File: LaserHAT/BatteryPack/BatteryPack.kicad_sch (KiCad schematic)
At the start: 140 parts, among them J1 TYPE-C-31-M-12, J3 B4B-PH-K-S(LF)(SN), J5 S5B-XH-A-1(LF)(SN), J6 S5B-XH-A-1(LF)(SN), J7 XT60PW-M, J8 XT60PW-M, Q1 AO3401A, Q10 AO3400A, Q11 AO3400A, Q12 AO3400A, Q13 AO3401A, Q14 AO3400A, Q15 AO3400A, Q16 AO3400A, Q17 AO3400A, Q18 AO3400A, Q6 AO3401A, Q7 AO3400A, Q8 AO3400A, Q9 AO3400A, SW1 CAX-MTS203M-YB-10.6JL, U1 LM393DR2G, U10 HY2213-BB3A, U11 HY2213-BB3A, U12 HY2213-BB3A, U13 HY2213-BB3A, U14 LM393DR2G, U15 LM393DR2G, U16 CJ431, U2 LM393DR2G, U3 CJ431, U4 CH224A, U5 CN3704, U6 HY2213-BB3A, U7 HY2213-BB3A, U8 HY2213-BB3A, U9 HY2213-BB3A

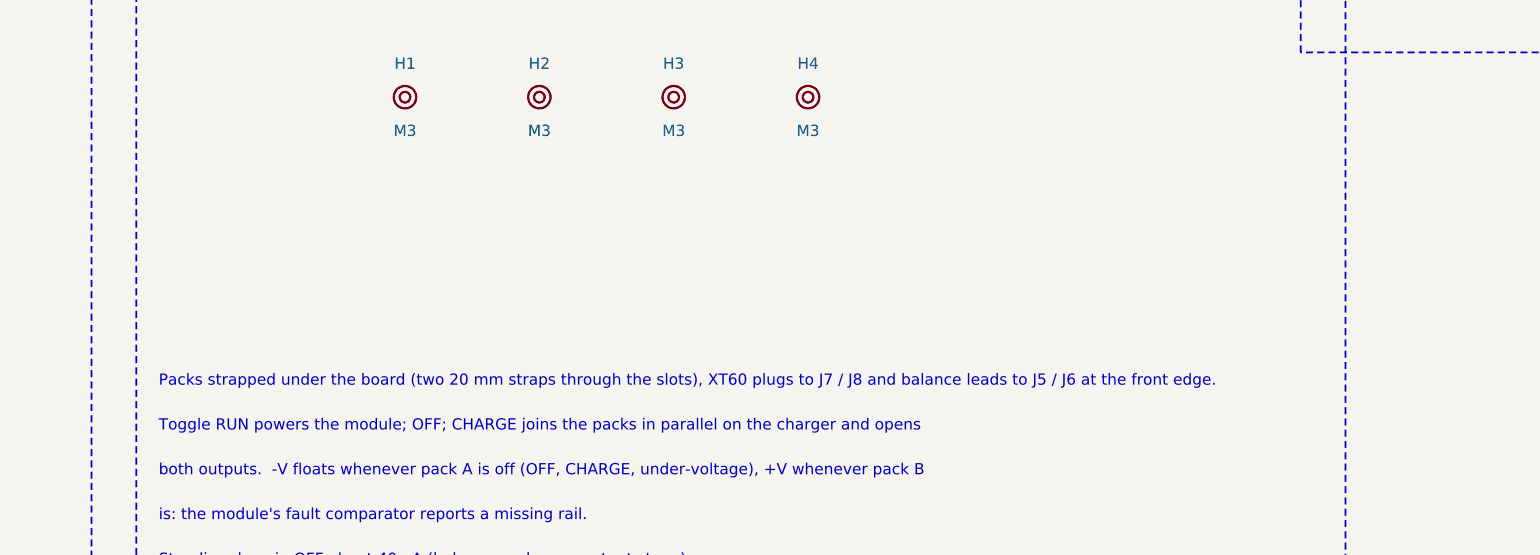
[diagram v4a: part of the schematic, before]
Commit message: BatteryPack: Raspberry Pi mounting holes (H5-H8, 58 x 49 M2.5) so the Pi + HAT sit above the board
Pi over y 4-60 on standoffs, ports end 11 mm past the right edge; toggle, pack sockets, output header and every
LED stay uncovered.  Balancer rows up 3 mm (pack B 1 mm left), CHRG / DONE LEDs to the top edge outside the Pi,
R9-R11 and C3 nudged, no-via rule areas under the standoffs.  Re-routed; one +SW pad entry hand-fixed for the
0.2 mm clearance.  DRC 0 / 0 / 0, ERC 0, path / sync 0, fab 136 placements / 44 BOM lines.

Co-Authored-By: Claude Fable 5.1 <noreply@anthropic.com>
Claude-Session: https://claude.ai/code/session_018vgLizGzYPynnY93ajvoVA
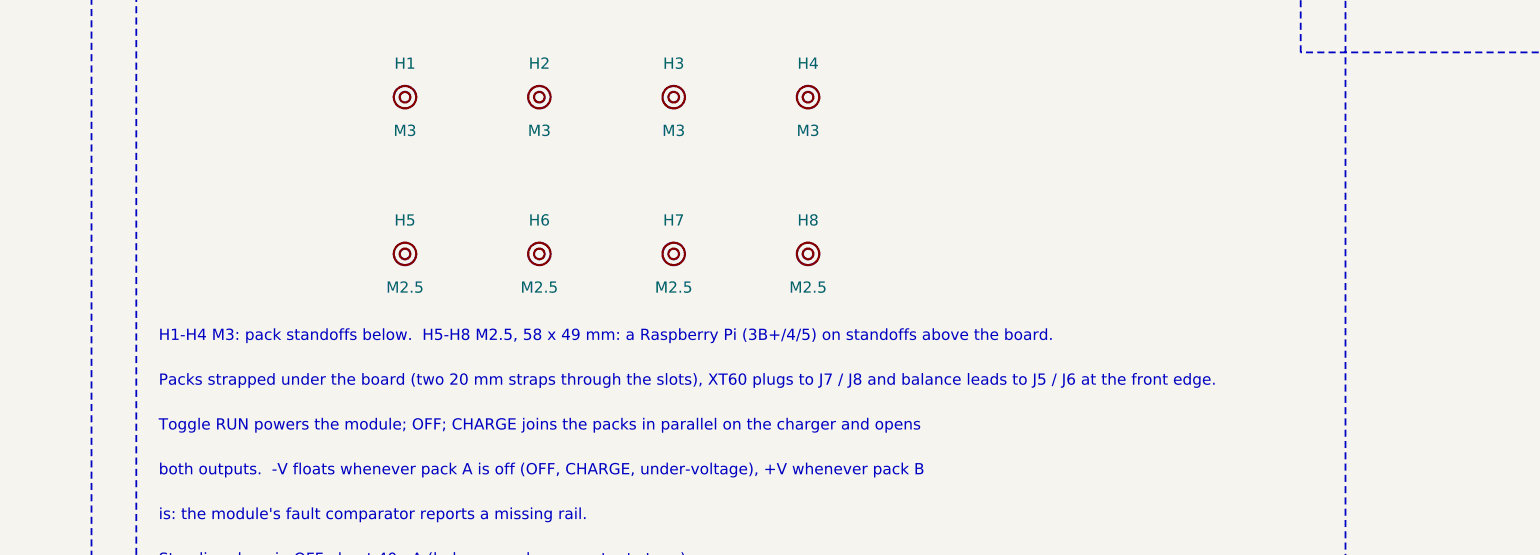
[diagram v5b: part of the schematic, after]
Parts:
- added H5, H6, H7, H8: M2.5, MountingHole:MountingHole_2.7mm_M2.5, symbol battpack:MountingHole
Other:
- note added: "H1-H4 M3: pack standoffs below. H5-H8 M2.5, 58 x 49 mm: a Raspberry Pi (3B+/4/5) on standoffs above the board."
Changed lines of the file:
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@@
     (instances (project "BatteryPack" (path "/15556796-a1bc-5b7f-a5a5-0a862d310368" (reference "H4") (unit 1))))
   )
+  (symbol (lib_id "battpack:MountingHole") (at 431.8 337.82 0) (unit 1) (exclude_from_sim no) (in_bom no) (on_board yes) (dnp no)
+    (property "Reference" "H5" (at 431.8 334.01  0) (effects (font (size 1.27 1.27)) ))
+    (property "Value" "M2.5" (at 431.8 341.63  0) (effects (font (size 1.27 1.27)) ))
+    (property "Footprint" "MountingHole:MountingHole_2.7mm_M2.5" (at 431.8 337.82 0) (effects (font (size 1.27 1.27)) (hide yes)))
+    (property "Datasheet" "" (at 431.8 337.82 0) (effects (font (size 1.27 1.27)) (hide yes)))
+    (instances (project "BatteryPack" (path "/15556796-a1bc-5b7f-a5a5-0a862d310368" (reference "H5") (unit 1))))
+  )
+  (symbol (lib_id "battpack:MountingHole") (at 447.04 337.82 0) (unit 1) (exclude_from_sim no) (in_bom no) (on_board yes) (dnp no)
+    (property "Reference" "H6" (at 447.04 334.01  0) (effects (font (size 1.27 1.27)) ))
+    (property "Value" "M2.5" (at 447.04 341.63  0) (effects (font (size 1.27 1.27)) ))
+    (property "Footprint" "MountingHole:MountingHole_2.7mm_M2.5" (at 447.04 337.82 0) (effects (font (size 1.27 1.27)) (hide yes)))
+    (property "Datasheet" "" (at 447.04 337.82 0) (effects (font (size 1.27 1.27)) (hide yes)))
+    (instances (project "BatteryPack" (path "/15556796-a1bc-5b7f-a5a5-0a862d310368" (reference "H6") (unit 1))))
+  )
+  (symbol (lib_id "battpack:MountingHole") (at 462.28 337.82 0) (unit 1) (exclude_from_sim no) (in_bom no) (on_board yes) (dnp no)
+    (property "Reference" "H7" (at 462.28 334.01  0) (effects (font (size 1.27 1.27)) ))
+    (property "Value" "M2.5" (at 462.28 341.63  0) (effects (font (size 1.27 1.27)) ))
+    (property "Footprint" "MountingHole:MountingHole_2.7mm_M2.5" (at 462.28 337.82 0) (effects (font (size 1.27 1.27)) (hide yes)))
+    (property "Datasheet" "" (at 462.28 337.82 0) (effects (font (size 1.27 1.27)) (hide yes)))
+    (instances (project "BatteryPack" (path "/15556796-a1bc-5b7f-a5a5-0a862d310368" (reference "H7") (unit 1))))
+  )
+  (symbol (lib_id "battpack:MountingHole") (at 477.52 337.82 0) (unit 1) (exclude_from_sim no) (in_bom no) (on_board yes) (dnp no)
+    (property "Reference" "H8" (at 477.52 334.01  0) (effects (font (size 1.27 1.27)) ))
+    (property "Value" "M2.5" (at 477.52 341.63  0) (effects (font (size 1.27 1.27)) ))
+    (property "Footprint" "MountingHole:MountingHole_2.7mm_M2.5" (at 477.52 337.82 0) (effects (font (size 1.27 1.27)) (hide yes)))
+    (property "Datasheet" "" (at 477.52 337.82 0) (effects (font (size 1.27 1.27)) (hide yes)))
+    (instances (project "BatteryPack" (path "/15556796-a1bc-5b7f-a5a5-0a862d310368" (reference "H8") (unit 1))))
+  )
+  (text "H1-H4 M3: pack standoffs below.  H5-H8 M2.5, 58 x 49 mm: a Raspberry Pi (3B+/4/5) on standoffs above the board." (exclude_from_sim no) (at 403.86 347.98 0) (effects (font (size 1.27 1.27)) (justify left bottom)))
   (text "Packs strapped under the board (two 20 mm straps through the slots), XT60 plugs to J7 / J8 and balance leads to J5 / J6 at the front edge." (exclude_from_sim no) (at 403.86 353.06 0) (effects (font (size 1.27 1.27)) (justify left bottom)))
   (text "Toggle RUN powers the module; OFF; CHARGE joins the packs in parallel on the charger and opens" (exclude_from_sim no) (at 403.86 358.14 0) (effects (font (size 1.27 1.27)) (justify left bottom)))

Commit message: BatteryPack rev D: packs in series, floating charger switched between them by a relay under an STM32F042, ON/OFF toggle, plug interlock, 0V pour
Rev C's parallel/series toggle made half the board jump by a pack voltage, needed a PTC link and an equalising rule, and left no single
reference.  Rev D keeps the packs in series for good (GND / 0V / +BATB), floats the whole charger on its own ground CGND and lets an
HFD2 relay under an STM32F042F4P6 (USB DFU, firmware/) connect it to pack A or pack B: "charge the lower pack" in 3-minute slots with
the CN3704 power-cycled at every reconnection, per-pack CHG / DONE LEDs.  MTS-202 ON/OFF toggle; +V is enabled only with the module's
plug in (J3 pin 4 strapped to 0V) because the module dies from +V / -V without 0V; an EL817 opto turns the outputs off while a brick
is in.  Gauge rails through P-FETs, ladder re-tuned for the undropped rail.

Layout mirror-symmetric about x = 50 with the Pi along the top edge (its USB-C / HDMI face flush, module over the top-right corner
above J3), the gauge LED columns paired in the centre (80 / 50 / 20 / ON / CHG / DONE), toggle and USB-C in the middle of the front,
relay front-right, PD sink front-left, charger island in the centre column under the Pi.  Freerouting + maze_route; back-side 0V
pour; DRC 0/0/0, path / sync 0, lcsc_check clean, fab outputs and renders regenerated.  Firmware compiles only with an ARM toolchain
(not present here); DFU on the TSSOP-20 and the relay's pick-up at 20 V are first-board checks (README).

Co-Authored-By: Claude Fable 5.1 <noreply@anthropic.com>
Claude-Session: https://claude.ai/code/session_018vgLizGzYPynnY93ajvoVA
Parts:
- removed D15, D16, D5, D6: SS14, Diode_SMD:D_SMA, symbol battpack:D_Schottky
- removed F3: MF-MSMF110/24X-2, Fuse:Fuse_1812_4532Metric, symbol battpack:Polyfuse
- removed R30: 1M, Resistor_SMD:R_0603_1608Metric, symbol battpack:R
- removed R41: 100k, Resistor_SMD:R_0603_1608Metric, symbol battpack:R
- added C22, C23: 1u, Capacitor_SMD:C_0603_1608Metric, symbol battpack:C
- added C24, C25, C26: 100n, Capacitor_SMD:C_0603_1608Metric, symbol battpack:C
- added D17: KT-0603R, LED_SMD:LED_0603_1608Metric, symbol battpack:LED
- added D18: KT-0805G, LED_SMD:LED_0805_2012Metric, symbol battpack:LED
- added D19: 1N4148W, Diode_SMD:D_SOD-123, symbol battpack:D
- added K1: HFD2/024-M, battpack:Relay_HFD2, symbol battpack:HFD2
- added Q19, Q21, Q22, Q24: 2N7002, Package_TO_SOT_SMD:SOT-23, symbol battpack:Q_NMOS_GSD
- added Q20, Q23: AO3401A, Package_TO_SOT_SMD:SOT-23, symbol battpack:Q_PMOS_GSD
- added R66, R68: 1k, Resistor_SMD:R_0603_1608Metric, symbol battpack:R
- added R67, R69: 470, Resistor_SMD:R_0603_1608Metric, symbol battpack:R
- added R70, R76: 10k, Resistor_SMD:R_0603_1608Metric, symbol battpack:R
- added R71, R73, R77, R78, R79, R80, R83, R84: 100k, Resistor_SMD:R_0603_1608Metric, symbol battpack:R
- added R72, R74: 18k, Resistor_SMD:R_0603_1608Metric, symbol battpack:R
- added R81, R82: 1M, Resistor_SMD:R_0603_1608Metric, symbol battpack:R
- added SW2: TS-1187A-B-A-B, Button_Switch_SMD:SW_Push_1P1T_XKB_TS-1187A, symbol battpack:SW_Push
- added TP1: SWDIO, TestPoint:TestPoint_Pad_1.5x1.5mm, symbol battpack:TestPoint
- added TP2: SWCLK, TestPoint:TestPoint_Pad_1.5x1.5mm, symbol battpack:TestPoint
- added TP3: CGND, TestPoint:TestPoint_Pad_1.5x1.5mm, symbol battpack:TestPoint
- added TP4: +3V3, TestPoint:TestPoint_Pad_1.5x1.5mm, symbol battpack:TestPoint
- added U17: EL817S1(C)(TU)-F, battpack:EL817S1, symbol battpack:EL817
- added U18: TLV76033DBZR, Package_TO_SOT_SMD:SOT-23, symbol battpack:TLV760
- added U19: STM32F042F4P6, Package_SO:TSSOP-20_4.4x6.5mm_P0.65mm, symbol battpack:STM32F042F4
- Q12: value AO3400A -> 2N7002; LCSC Part # C20917 -> C8545
- R28, R29: value 15k -> 10k; LCSC Part # C22809 -> C25804
- R4, R46: value 6.8k -> 6.2k; LCSC Part # C23212 -> C4260
- SW1: value CAX-MTS203M-YB-10.6JL -> CAX-MTS202B2-BB-20.5JL; footprint battpack:SW_MTS-203 -> battpack:SW_MTS-202; symbol battpack:SW_DPDT_CO -> battpack:SW_DPDT; LCSC Part # C55160018 -> C55159891
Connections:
- net +RUN is gone; now on net +BATB: F1.1, SW1.4 (A2)
- net +BATB: now also K1.8 (NO1), Q23.2 (S), R83.1; no longer SW1.5 (C2)
- net +G: now also Q20.3 (D)
- net +GB: now also Q23.3 (D)
- net 0V: now also J5.5 (Pin_5), J7.2 (Pin_2), R34.1, R38.1, SW1.1 (A1), K1.6 (NC1), K1.9 (NO2), Q20.2 (S), Q24.2 (S), R77.1, R82.2, U17.3 (E); no longer R39.1, SW1.2 (C1)
- net CHRG: now also R28.2, U19.8 (PA2); no longer D9.1 (K)
- net DONE: now also R29.2, U19.9 (PA3); no longer D10.1 (K)
- net GND: now also K1.11 (NC2), Q21.2 (S), R80.2; no longer C10.2, C11.2, C3.2, C5.2 (-), C6.2, C7.2, C8.2, C9.2, D8.2 (A), J1.A1 (GND), J1.A12 (GND), J1.B1 (GND), J1.B12 (GND), J1.S1 (SH), Q12.2 (S), R24.2, R42.2, RT1.2, SW1.3 (B1), U4.11 (GND), U5.10 (test), U5.2 (PGND), U5.3 (GND), U5.7 (EOC)
- net THCUTB: now also U15.6 (-); no longer U15.5 (+)
- net VBUS: now also C22.1, D19.1 (K), K1.1 (+), R73.1, R76.1, U18.2 (IN)
- net VCHG: no longer R28.1, R29.1
- net VSB: now also U15.5 (+); no longer U15.6 (-)
- net at D9.2 (A): now also R66.2; no longer R28.2
- net at D10.2 (A): now also R67.2; no longer R29.2
- net USB_DP: now reaches J1.A6 (D+), J1.B6 (D+)
- net USB_DP: now also U19.18 (PA10/USB_DP); no longer U4.4 (DP)
- net USB_DM: now reaches J1.A7 (D-), J1.B7 (D-)
- net USB_DM: now also U19.17 (PA9/USB_DM); no longer U4.5 (DM)
- net CAB: now reaches J3.4 (Pin_4)
- net CAB: now also Q22.2 (S)
- removed net +BAT: C7.1, C8.1, J5.5 (Pin_5), J7.2 (Pin_2), R26.2, R34.1, R38.1, SW1.1 (A1), U5.14 (BAT)
- net +CHGB: no longer names the net of SW1.6 (B2)
- net CUT_OCB renamed ENB_G
- net ENB_G: now also Q22.1 (G), R81.2, U17.4 (C); no longer R2.2
- net Q12_G renamed CHG_EN
- net CHG_EN: now also U19.11 (PA5)
- new net: R76.2, U17.1 (A)
- new net: D17.2 (A), R68.2
- new net: D18.2 (A), R69.2
- new net +3V3: C23.1, C24.1, C25.1, R28.1, R29.1, SW2.2, TP4.1, U18.1 (OUT), U19.16 (VDD), U19.5 (VDDA)
- new net +CHG: C7.1, C8.1, K1.4 (COM1), R26.2, R71.1, U5.14 (BAT)
- new net BOOT0: R70.1, SW2.1, U19.1 (BOOT0)
- new net CGND: C10.2, C11.2, C22.2, C23.2, C24.2, C25.2, C26.2, C3.2, C5.2 (-), C6.2, C7.2, C8.2, C9.2, D10.1 (K), D17.1 (K), D18.1 (K), D8.2 (A), D9.1 (K), J1.A1 (GND), J1.A12 (GND), J1.B1 (GND), J1.B12 (GND), J1.S1 (SH), K1.13 (COM2), Q12.2 (S), Q19.2 (S), R24.2, R42.2, R70.2, R72.2, R74.2, RT1.2, TP3.1, U17.2 (K), U18.3 (GND), U19.15 (VSS), U4.11 (GND), U5.10 (test), U5.2 (PGND), U5.3 (GND), U5.7 (EOC)
- new net EN_A: R39.1, R79.1, SW1.2 (C1)
- new net EN_B: Q24.1 (G), R81.1, R82.1, SW1.5 (C2)
- new net LED_CA: R66.1, U19.12 (PA6)
- new net LED_CB: R68.1, U19.14 (PB1)
- new net LED_DA: R67.1, U19.13 (PA7)
- new net LED_DB: R69.1, U19.2 (PF0)
- new net NRST: C26.1, U19.4 (NRST)
- new net Q20_G: Q20.1 (G), R77.2, R78.1
- new net Q21_D: Q21.3 (D), R78.2
- new net Q21_G: Q21.1 (G), R79.2, R80.1
- new net Q22_D: Q22.3 (D), R2.2
- new net Q23_G: Q23.1 (G), R83.2, R84.1
- new net Q24_D: Q24.3 (D), R84.2
- new net RELAY: Q19.1 (G), U19.10 (PA4)
- new net RLY_K: D19.2 (A), K1.16 (-), Q19.3 (D)
- new net SWCLK: TP2.1, U19.20 (PA14/SWCLK)
- new net SWDIO: TP1.1, U19.19 (PA13/SWDIO)
- new net VBAT_S: R71.2, R72.1, U19.6 (PA0)
- new net VBUS_S: R73.2, R74.1, U19.7 (PA1)
- no-connect marks 31 -> 35
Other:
- note added: "(board temperature; a 10k resistor disables it). CHRG / DONE are read by the MCU. Up to 2 A: R25 + R26 = 0.1 R, L1 20 uH, 45 W brick."
- note added: "-V floats whenever pack A is off (OFF, under-voltage), +V whenever pack B is or the plug is out or a"
- note added: "1. TWO 4S PACKS IN SERIES: XT60 DISCHARGE PLUGS (J7 / J8, run + charge current) AND JST-XH BALANCE LEADS (pin 1 = black = pack negative), PER-CELL BALANCERS (HY2213-BB3A, 42 mA above 4.20 V)"
- note added: "16.8 V +-1 % constant voltage, termination at 9 % (92 mA), trickle at 150 mA below 11.2 V, over-voltage cut at 18.1 V. RT1 10k NTC"
- note added: "2. ON / OFF TOGGLE, OUTPUT CHAINS (+V: Q1, -V: Q11), PLUG INTERLOCK (Q22), CHARGING INTERLOCK (U17)"
- note added: "2B. GAUGE RAILS: +G = 0V THROUGH Q20, +GB = +BATB THROUGH Q23"
- note added: "40 uA on the packs (balancers, charger sleep). A brick plugged in disables the outputs (U17)."
- note added: "6. CHARGER ISLAND (floats on CGND): USB-C PD 20 V INPUT (CH224A), 3.3 V (TLV760), VBUS SWITCH (MCU), 4S BUCK CHARGER (CN3704, 1 A)"
- note added: "7. CHARGE CONTROLLER (island): STM32F042F4P6 (USB DFU), RELAY K1 TO PACK A / B, PER-PACK CHARGING / DONE LEDs"
- note added: "Any 4S LiPo / Li-ion hobby pack with a JST-XH 2.5 mm 5-pin balance plug and an XT60 discharge plug. Pack A's positive and pack B's negative are one node, 0V, the output reference: the"
- note added: "D4 >= 15.9 V (80 %), D3 >= 15.1 V (50 %), D2 >= 14.3 V (20 %) from +G; D1 (ON) lit by Q14 while Q11 conducts (-V live)."
- note added: "D7 blocks the pack from the input, D8 freewheels, L1 22 uH, R25 + R26 = 0.2 R -> 1 A constant current into one pack at a time,"
- note added: "D9 / D10 = pack A charging / done, D17 / D18 = pack B. Program: hold SW2, plug into a PC, dfu-util (firmware/); or SWD on TP1 / TP2."
- note added: "Everything in this box and in box 7 is referenced to CGND, which the relay K1 puts on GND (pack A) or on 0V (pack B); the brick is"
- note added: "J3 pin 4 (CAB) is strapped to pin 2 (0V) inside the module's plug: +V is enabled only with the plug in, so"
- note added: "Ladder (108 uA): TH80 2.162 V, TH50 2.054 V, TH20 1.946 V, THCUT 1.613 V. VS = rail x 0.1357 with the output live, x 0.1271 cut off; the rail is the pack itself (P-FET)."
- note added: "OUT: +V / 0V / -V / CAB (JST-PH 4, to the module)"
- note added: "PACK A (-V side): GND .. 0V"
- note added: "SW1 ON: pole 1 puts EN_A at 0V (= pack A positive), pole 2 puts EN_B at +BATB; OFF opens both (R40 / R82 hold them low). Chain B: Q22 (2N7002) conducts when ENB_G is high"
- note added: "Thresholds 15.9 / 15.1 / 14.3 V (pack) for the 80 / 50 / 20 % LEDs, cutoff 11.9 V, re-enable 12.7 V (pack B, R53 from +OUT) / 12.8 V (pack A, R11 from Q11's gate)."
- note added: "U15B below 12.0 V (back above 12.8 V: R53 from +OUT) and by U17 while a brick is plugged in. Chain A: Q11 (N, in pack A's negative) gets Vgs = pack A / 2 from R39 / R40 off EN_A;"
- note added: "U19 runs the charge: at every slot end it pauses the charger (CHG_EN low), reads the connected pack at rest (R71 / R72), compares it with the other"
- note added: "U2B pulls the gate low below 12.0 V (R11 470k: back on at 12.9 V). -V without 0V is harmless to the module, +V without 0V kills it, so only +V is interlocked (and the"
- note added: "and its source, J3.4, is at 0V, i.e. the module's plug is in (it straps pin 4 to pin 2): then R1 / R2 give Q1 Vgs = -Vsw/2 and +V is live. ENB_G = EN_B through R81 1M, pulled to 0V by"
- note added: "brick is in: the module's fault comparator reports a missing rail."
- note added: "mains-isolated, so the island floating is fine. J1 / U4: the CH224A asks a PD brick for 20 V (R24 120k on CFG1); its DP / DM stay"
- note added: "module's fault line reports a missing rail either way). Gauge rails (box 2B) follow EN_A / EN_B, not the interlocks: both gauges show whenever the toggle is ON."
- note added: "open, the USB data lines go to the MCU (DFU). U18 makes 3.3 V from VBUS (5 V from a PC port, 20 V from the brick). Q13 passes VBUS"
- note added: "pack's last resting reading and keeps or swaps the relay (RELAY high = pack B), then restarts the charger. DONE flags the pack as full; both full = idle."
- note added: "packs are never reconfigured. Balancer per cell: HY2213 OUT drives an AO3400A that bleeds the cell through 100 R (42 mA, 0.18 W) above 4.200 V, off at 4.19 V; 2.5 uA standing."
- note added: "so the CN3704 starts a fresh cycle (it would not restart on a pack above its 16.0 V recharge threshold). U5: buck at 300 kHz, Q6 switch,"
- note added: "the module never sees +V without 0V. Toggle ON powers the module and the gauges; OFF leaves about"
- note added: "to the charger only while the MCU drives CHG_EN (R42 keeps it off in reset / DFU): the MCU power-cycles the charger at every pack swap"
- note removed: "+GB = +SW or +CHGB (D5/D6), +G = 0V or +CHGB (D15/D16): both gauges run in RUN and CHARGE and are dead in OFF."
- note removed: "1. TWO 4S PACKS: XT60 DISCHARGE PLUGS (J7 / J8, run + charge current) AND JST-XH BALANCE LEADS (pin 1 = black = pack negative), PER-CELL BALANCERS (HY2213-BB3A, 42 mA above 4.20 V)"
- note removed: "2. RUN / OFF / CHARGE TOGGLE, OUTPUT CHAINS (+V: Q1, -V: Q11), PARALLEL LINK FOR CHARGING"
- note removed: "6. USB-C PD 20 V INPUT (CH224A), VBUS SWITCH (CHARGE ONLY), 4S BUCK CHARGER (CN3704, 1 A)"
- note removed: "9 % (92 mA), trickle at 150 mA below 11.2 V, re-charge below 16.0 V, over-voltage cut at 18.1 V. RT1 10k NTC (board temperature; a 10k"
- note removed: "Any 4S LiPo / Li-ion hobby pack with a JST-XH 2.5 mm 5-pin balance plug and an XT60 discharge plug. Balancer per cell: HY2213 OUT drives an AO3400A that bleeds the cell"
- note removed: "CHARGE); a brick plugged in while RUN or OFF does nothing. U5: buck at 300 kHz, Q6 switch, D7 blocks the packs from the input, D8 freewheels,"
- note removed: "D4 >= 16.0 V (80 %), D3 >= 15.2 V (50 %), D2 >= 14.4 V (20 %) from +G; D1 (ON) lit by Q14 while Q11 conducts (-V live)."
- note removed: "J1 / U4: the CH224A asks a PD brick for 20 V (R24 120k on CFG1). Q13 passes VBUS to the charger only while Q12 sees +CHGB (toggle in"
- note removed: "L1 22 uH, R25 + R26 = 0.2 R -> 1 A constant current shared by the two packs in parallel (F3), 16.8 V +-1 % constant voltage, termination at"
- note removed: "Ladder (107 uA): TH80 2.137 V, TH50 2.029 V, TH20 1.920 V, THCUT 1.595 V. VS = rail x 0.1357 with the output live, x 0.1271 cut off; rail = pack - 0.25 V (SS14)."
- note removed: "OUT: +V / 0V / -V / nc (JST-PH 4, to the module)"
- note removed: "PACK A (-V side): GND .. +BAT"
- note removed: "R30 holds 0V at GND. Q1: U15B pulls the gate low (R1/R2) while VSB > THCUTB. Q11 (N, on pack A's negative): R39 from 0V and R40 give Vgs = +BAT/2 in RUN;"
- note removed: "RUN -> +RUN -> F1 -> +SW -> Q1 -> +OUT (+V); CHARGE -> +CHGB -> F3 (1.1 A PTC) -> +BAT (positives joined: both packs on the one charger). OFF opens both,"
- note removed: "SW1 pole 1 (common 0V = pack B negative): RUN -> +BAT (packs in series, 0V = output 0 V); CHARGE -> GND (negatives joined). Pole 2 (common +BATB):"
- note removed: "Standing draw in OFF about 40 uA (balancers, charger output stage)."
- note removed: "Thresholds 16.0 / 15.2 / 14.4 V (pack) for the 80 / 50 / 20 % LEDs, cutoff 12.0 V, re-enable 12.8 V (pack B, R53 from +OUT) / 12.9 V (pack A, R11 from Q11's gate)."
- note removed: "Toggle RUN powers the module; OFF; CHARGE joins the packs in parallel on the charger and opens"
- note removed: "U2B pulls the gate low below 12.0 V (R11 470k from the gate: back on at 12.9 V); in OFF and CHARGE 0V is at GND, so Q11 is off and -V floats. Gauge rails:"
- note removed: "both outputs. -V floats whenever pack A is off (OFF, CHARGE, under-voltage), +V whenever pack B"
- note removed: "is: the module's fault comparator reports a missing rail."
- note removed: "resistor disables it). D9 CHRG (red), D10 DONE (green). All of it on GND = pack A negative = the USB-C shell."
- note removed: "through 100 R (42 mA, 0.18 W) above 4.200 V, off at 4.19 V; 2.5 uA standing. With the charger's 16.8 V this is the balance. Pack B's negative is the 0 V output node."
- title: Battery board for the LaserHAT e-stim module: two 4S hobby packs, one charger -> Battery board for the LaserHAT e-stim module: two 4S hobby packs in series, one floating charger
- moved on the sheet: D10, D9, F2, Q11, R28, R29, R39, R40, R42, U15B, U2B

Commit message: BatteryPack rev D: audit fixes (relay, output socket, standby drain, relay pull-down, decoupling), re-routed
A layout audit found the home-made HFD2 relay footprint mirrored (the datasheet's PCB layout is a bottom view) with the coil
reversed, and the 24 V coil's 18 V pick-up had no margin on a 20 V bus.  Relay is now an Omron G6S-2 DC12 on KiCad's library
footprint, its 12 V coil fed through 680 R (R86), with R85 holding the driver off in reset / DFU and the flyback across the
coil.  The HFD2 footprint is corrected but unused.  Also from the audit: the pack-sense divider is 1M / 180k + 100n (it drew
140 uA from pack A whenever the brick was out and back-powered the MCU), J3 is a side-entry PH socket opening over the top
edge (a vertical header 2-7 mm inside the Pi's edge could not bend the cable in 3.5 mm), the BOOT button sits in the front
strip, the CH224A's 1 uF is beside it, the buck's freewheel diode and 1 uF are beside the switch, the VDDA cap is at its pin,
C7 / C8 are 22 uF 1206.  Re-placed and re-routed from scratch; DRC 0/0 with the 0V pour, path / sync 0, LCSC codes verified,
fab outputs and renders regenerated.

Co-Authored-By: Claude Fable 5.1 <noreply@anthropic.com>
Claude-Session: https://claude.ai/code/session_018vgLizGzYPynnY93ajvoVA
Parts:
- added C27: 100n, Capacitor_SMD:C_0603_1608Metric, symbol battpack:C
- added R85: 100k, Resistor_SMD:R_0603_1608Metric, symbol battpack:R
- added R86: 680, Resistor_SMD:R_0805_2012Metric, symbol battpack:R
- C7, C8: value 10u -> 22u; footprint Capacitor_SMD:C_0805_2012Metric -> Capacitor_SMD:C_1206_3216Metric; LCSC Part # C15850 -> C12891
- J3: value B4B-PH-K-S(LF)(SN) -> S4B-PH-K-S(LF)(SN); footprint Connector_JST:JST_PH_B4B-PH-K_1x04_P2.00mm_Vertical -> Connector_JST:JST_PH_S4B-PH-K_1x04_P2.00mm_Horizontal; LCSC Part # C131334 -> C157926
- K1: value HFD2/024-M -> G6S-2 DC12; footprint battpack:Relay_HFD2 -> Relay_THT:Relay_DPDT_Omron_G6S-2; symbol battpack:HFD2 -> battpack:G6S2; LCSC Part # C18198081 -> C1525289
- R71: value 100k -> 1M; LCSC Part # C25803 -> C22935
- R72: value 18k -> 180k; LCSC Part # C25810 -> C22827
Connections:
- net +BATB: now also K1.5 (NO1); no longer K1.8 (NO1)
- net 0V: now also K1.3 (NC1), K1.8 (NO2); no longer K1.6 (NC1), K1.9 (NO2)
- net CGND: now also K1.9 (COM2), C27.2, R85.2; no longer K1.13 (COM2)
- net GND: now also K1.10 (NC2); no longer K1.11 (NC2)
- net RELAY: now also R85.1
- net RLY_K: now also K1.12 (-); no longer K1.16 (-)
- net VBAT_S: now also C27.1
- net VBUS: now also R86.1; no longer D19.1 (K), K1.1 (+)
- new net RLY_P: D19.1 (K), K1.1 (+), R86.2
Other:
- note added: "D9 / D10 = pack A charging / done, D17 / D18 = pack B. K1 G6S-2 12 V coil through R86 680 R from VBUS (11.7 mA; must-operate 9 V). Program: hold SW2, plug into a PC, dfu-util; or SWD on TP1 / TP2."
- note removed: "D9 / D10 = pack A charging / done, D17 / D18 = pack B. Program: hold SW2, plug into a PC, dfu-util (firmware/); or SWD on TP1 / TP2."
- moved on the sheet: D19

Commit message: BatteryPack rev D: second audit - K2 LINK relay isolates the charger while K1 moves, 33 uH, soft start, XT60 drills, JLC CPL rotations, HV clearance rules
A fresh, independent audit found that a single DPDT relay's poles are not
guaranteed to transfer together: with the charger island still tied to one
pack, the mismatched intermediate states put 33.6 V across the charger or short
its output capacitors through the contacts.  K2 (second G6S-2, both poles NO in
series with +CHG / CGND, PF1) now isolates the island while K1 moves; the
firmware opens K2, moves K1, closes K2, and keeps K2 open when idle, so the
island is off both packs at rest.

Also from the audit: L1 22 -> 33 uH (CN3704 table), C28 10 nF soft start on the
VBUS switch gate, R86/R88 680 R to 1206, XT60PW-M drills to Amass's 2025
drawing, CPL rotations corrected with the Fabrication Toolkit table
(make_fab.py wrote raw KiCad angles), 0.3 mm between Power-class nets on tracks
and 0.5 mm for the 33 V pairs (BatteryPack.kicad_dru), BRICK_MV 18 V, TP3 silk
CGND, RT1 moved clear of U5's bottom pins.  XT60 polarity documented as the
KiCad / hobby convention with the meter check kept as a first-board item.

Routing: autoroute.py now gives every pad of U5 / U19 a 0.2 mm escape stub and
takes locked pre-routes from route/preroute.json (the -V run along the top
edge); Freerouting + maze for the last ground links.  DRC 0/0 with the 0V pour,
path/sync 0, ERC 0, fab 175 placements / 54 BOM lines.

Co-Authored-By: Claude Fable 5.1 <noreply@anthropic.com>
Claude-Session: https://claude.ai/code/session_018vgLizGzYPynnY93ajvoVA
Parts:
- added C28: 10n, Capacitor_SMD:C_0603_1608Metric, symbol battpack:C
- added D20: 1N4148W, Diode_SMD:D_SOD-123, symbol battpack:D
- added K2: G6S-2 DC12, Relay_THT:Relay_DPDT_Omron_G6S-2, symbol battpack:G6S2
- added Q25: 2N7002, Package_TO_SOT_SMD:SOT-23, symbol battpack:Q_NMOS_GSD
- added R87: 100k, Resistor_SMD:R_0603_1608Metric, symbol battpack:R
- added R88: 680, Resistor_SMD:R_1206_3216Metric, symbol battpack:R
- L1: value MWSA0603S-220MT -> MWSA0603S-330MT; LCSC Part # C408453 -> C408454
- R86: footprint Resistor_SMD:R_0805_2012Metric -> Resistor_SMD:R_1206_3216Metric; LCSC Part # C17798 -> C17975
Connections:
- net +CHG: now also K2.4 (COM1); no longer K1.4 (COM1)
- net CGND: now also K2.9 (COM2), Q25.2 (S), R87.2; no longer K1.9 (COM2)
- net Q13_G: now also C28.2
- net VBUS: now also C28.1, R88.1
- net LINK: now reaches U19.3 (PF1)
- net LINK: now also Q25.1 (G), R87.1
- new net CGND_K: K1.9 (COM2), K2.8 (NO2)
- new net CHG_K: K1.4 (COM1), K2.5 (NO1)
- new net RLY2_K: D20.2 (A), K2.12 (-), Q25.3 (D)
- new net RLY2_P: D20.1 (K), K2.1 (+), R88.2
- no-connect marks 35 -> 36
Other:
- note added: "7B. LINK RELAY K2: ISOLATES THE ISLAND WHILE K1 MOVES (a DPDT's poles are not simultaneous); THE ALGORITHM"
- note added: "DONE flags a pack full; both full = idle with K2 open. Coils: 12 V through 680 R from VBUS (11.7 mA each; must-operate 9 V). Program: SW2 + dfu-util, or SWD."
- note added: "U19 runs the charge: at every slot end it pauses the charger (CHG_EN low), reads the connected pack at rest (R71 / R72) and compares it"
- note added: "with the other pack's last resting reading; to swap it opens K2, moves K1 (RELAY high = pack B), closes K2 and restarts the charger."
- note removed: "D9 / D10 = pack A charging / done, D17 / D18 = pack B. K1 G6S-2 12 V coil through R86 680 R from VBUS (11.7 mA; must-operate 9 V). Program: hold SW2, plug into a PC, dfu-util; or SWD on TP1 / TP2."
- note removed: "U19 runs the charge: at every slot end it pauses the charger (CHG_EN low), reads the connected pack at rest (R71 / R72), compares it with the other"
- note removed: "pack's last resting reading and keeps or swaps the relay (RELAY high = pack B), then restarts the charger. DONE flags the pack as full; both full = idle."
